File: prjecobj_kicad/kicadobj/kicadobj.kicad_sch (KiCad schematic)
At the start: 39 parts, among them U1 ESP32-S3-DevKitC, U2 PCM1808PWR, U3 MAX9812, U5 PJ-342B

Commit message: feat(prjecobj_kicad)[sang]: update old schematics into new prototype using LTSpice design
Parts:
- removed C1, C2: 0.1uF, Capacitor_SMD:C_0805_2012Metric, symbol Device:C
- removed C10, C14: 10uF, Capacitor_SMD:C_0805_2012Metric, symbol Device:C
- removed C15, C3: 1uF, Capacitor_SMD:C_0805_2012Metric, symbol Device:C
- removed MK1: Microphone, Sensor_Audio:POM-2244P-C3310-2-R, symbol Device:Microphone
- removed MK2: MP45DT02, Sensor_Audio:ST_HLGA-6_3.76x4.72mm_P1.65mm, symbol Sensor_Audio:MP45DT02
- removed unit 2 of Op-amp2
- removed unit 1 of Op-amp2
- removed R1, R14: 2.2kOhm, Resistor_SMD:R_0805_2012Metric, symbol Device:R_US
- removed R10, R11, R4: 10kOhm, Resistor_SMD:R_0805_2012Metric, symbol Device:R_US
- removed R12: 1MOhm, Resistor_SMD:R_0805_2012Metric, symbol Device:R_US
- removed R13, R7: 100kOhm, Resistor_SMD:R_0805_2012Metric, symbol Device:R_US
- removed R15, R5, R6: 1kOhm, Resistor_SMD:R_0805_2012Metric, symbol Device:R_US
- removed U3: MAX9812, max9812:21-0077G, symbol MAX9812:MAX9812
- added C23, C31: 1uF, Capacitor_SMD:C_0805_2012Metric, symbol Device:C
- added C25, C26, C30: 10uF, Capacitor_SMD:C_0805_2012Metric, symbol Device:C
- added C27, C28: 0.1uF, Capacitor_SMD:C_0805_2012Metric, symbol Device:C
- added C29: 1nF, Capacitor_SMD:C_0805_2012Metric, symbol Device:C
- added MK2: Microphone, Sensor_Audio:POM-2244P-C3310-2-R, symbol Device:Microphone
- added Op-amp3: TL072, TL072IDT:SOIC127P600X175-8N, symbol Amplifier_Operational:TL072
- added R26, R27, R29: 100kOhm, Resistor_SMD:R_0805_2012Metric, symbol Device:R_US
- added R28: 2.2kOhm, Resistor_SMD:R_0805_2012Metric, symbol Device:R_US
- added R30: 30kOhm, Resistor_SMD:R_0805_2012Metric, symbol Device:R_US
- added R31: 1kOhm, Resistor_SMD:R_0805_2012Metric, symbol Device:R_US
- added R32: 10kOhm, Resistor_SMD:R_0805_2012Metric, symbol Device:R_US
- added R33, R34: 60kOhm, Resistor_SMD:R_0805_2012Metric, symbol Device:R_US
- added U6: MAX9812, max9812:21-0077G, symbol MAX9812:MAX9812
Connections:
- net 12V: now also R27.1
- net 3.3V: now also C27.1, U6.1 (*SHDN), U6.4 (VCC)
- net GND: now also U5.2, C25.2, C27.2, C29.1, C30.1, C31.2, MK2.1 (-), R28.2, R29.1, U6.2 (GND); no longer U5.3
- net at U2.13 (VINL): now also C13.2, R2.2, R3.1, R33.1, R34.2
- net at U2.14 (VINR): now also C31.1, R34.1
- net at U1.12 (GPIO8/ADC1_CH7): no longer U5.2
- net at U5.4: now also U6.3 (OUT)
- new net: C30.2, R32.1
- new net: C26.1, R33.2
- new net: C26.2, Op-amp3.6 (-), Op-amp3.7
- new net: C25.1, R26.1, R27.2, R29.2
- new net: C23.2, Op-amp3.3 (+), R26.2
- new net: R28.1, U6.5 (BIAS)
- new net: C23.1, U5.3
- new net: C29.2, Op-amp3.5 (+), R31.1
- new net: C28.2, MK2.2 (+)
- new net: C28.1, U6.6 (IN)
- new net: Op-amp3.2 (-), R30.2, R32.2
- new net: Op-amp3.1, R30.1, R31.2
- no-connect marks 38 -> 41
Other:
- moved on the sheet: Op-amp2C, U5

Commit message: feat(kicad): update schematics and ad new PCB design with remove PCM1808 item and replace with pin connector
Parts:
- removed C27, C28, C5, C7, C9: 0.1uF, Capacitor_SMD:C_0805_2012Metric, symbol Device:C
- removed C4, C6, C8: 10uF, Capacitor_SMD:C_0805_2012Metric, symbol Device:C
- removed MK2: Microphone, Sensor_Audio:POM-2244P-C3310-2-R, symbol Device:Microphone
- removed Op-amp2: TL072, TL072IDT:SOIC127P600X175-8N, symbol Amplifier_Operational:TL072
- removed R28: 2.2kOhm, Resistor_SMD:R_0805_2012Metric, symbol Device:R_US
- removed U1: ESP32-S3-DevKitC, PCM_Espressif:ESP32-S3-DevKitC, symbol PCM_Espressif:ESP32-S3-DevKitC
- removed U2: PCM1808PWR, pcm1808-pwr:SOP65P640X120-14N, symbol PCM1808PWR:PCM1808PWR
- removed U6: MAX9812, max9812:21-0077G, symbol MAX9812:MAX9812
- added J1: MAX9812_Con_Pin_0103_V, Connector_PinHeader_2.54mm:PinHeader_1x03_P2.54mm_Vertical, symbol Connector_Generic:Conn_01x03
- added J2, J3: Conn_01x05, Connector_PinHeader_2.54mm:PinHeader_1x05_P2.54mm_Vertical, symbol Connector_Generic:Conn_01x05
- added J4: PCM1808_Con_Pin_0103_V, Connector_PinHeader_2.54mm:PinHeader_1x03_P2.54mm_Vertical, symbol Connector_Generic:Conn_01x03
- added unit 3 of Op-amp3
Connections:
- net 12V: now also Op-amp3.8 (V+)
- net 3.3V: now also J1.1 (Pin_1), J2.4 (Pin_4), J3.1 (Pin_1)
- net 5V: now also J2.5 (Pin_5)
- net GND: now also J2.3 (Pin_3), J3.2 (Pin_2), Op-amp3.4 (V-)
- net at C13.2, R2.2, R3.1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: now also J4.1 (Pin_1)
- net at C31.1, R34.1: now also J4.3 (Pin_3)
- net at INVBUF1.4, R8.2, R9.2: now also J3.3 (Pin_3)
- net at U5.4: now also J1.3 (Pin_3)
- no-connect marks 41 -> 16
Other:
- note added: "+3.3"
- note added: "+5"
- note added: "BCK"
- note added: "GND"
- note added: "LIN"
- note added: "LRC"
- note added: "MD0"
- note added: "MD1"
- note added: "OUT"
- note added: "PMT"
- note added: "RIN"
- note added: "SCK"

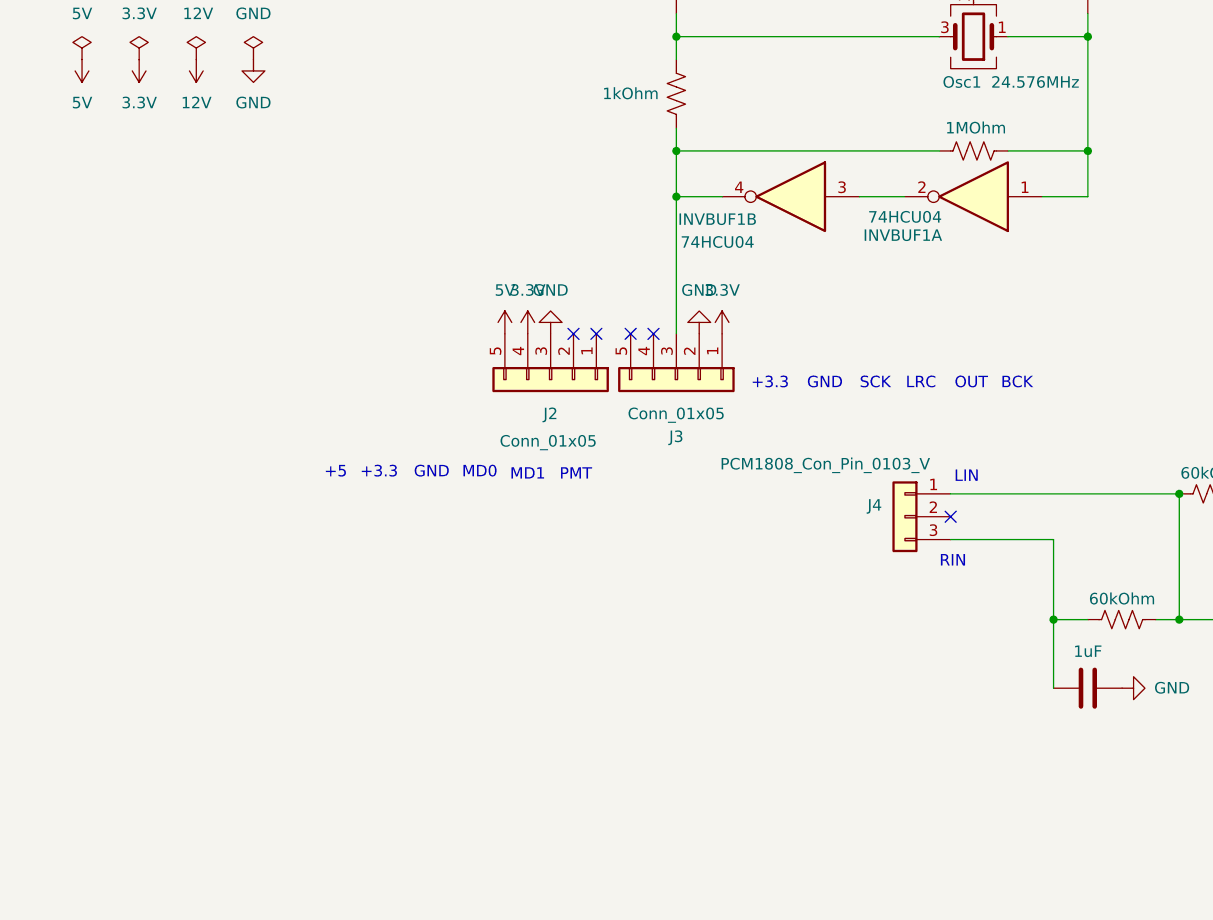
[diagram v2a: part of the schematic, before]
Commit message: feat(kicad): update connector from 1x5 to 1x6 with adding net
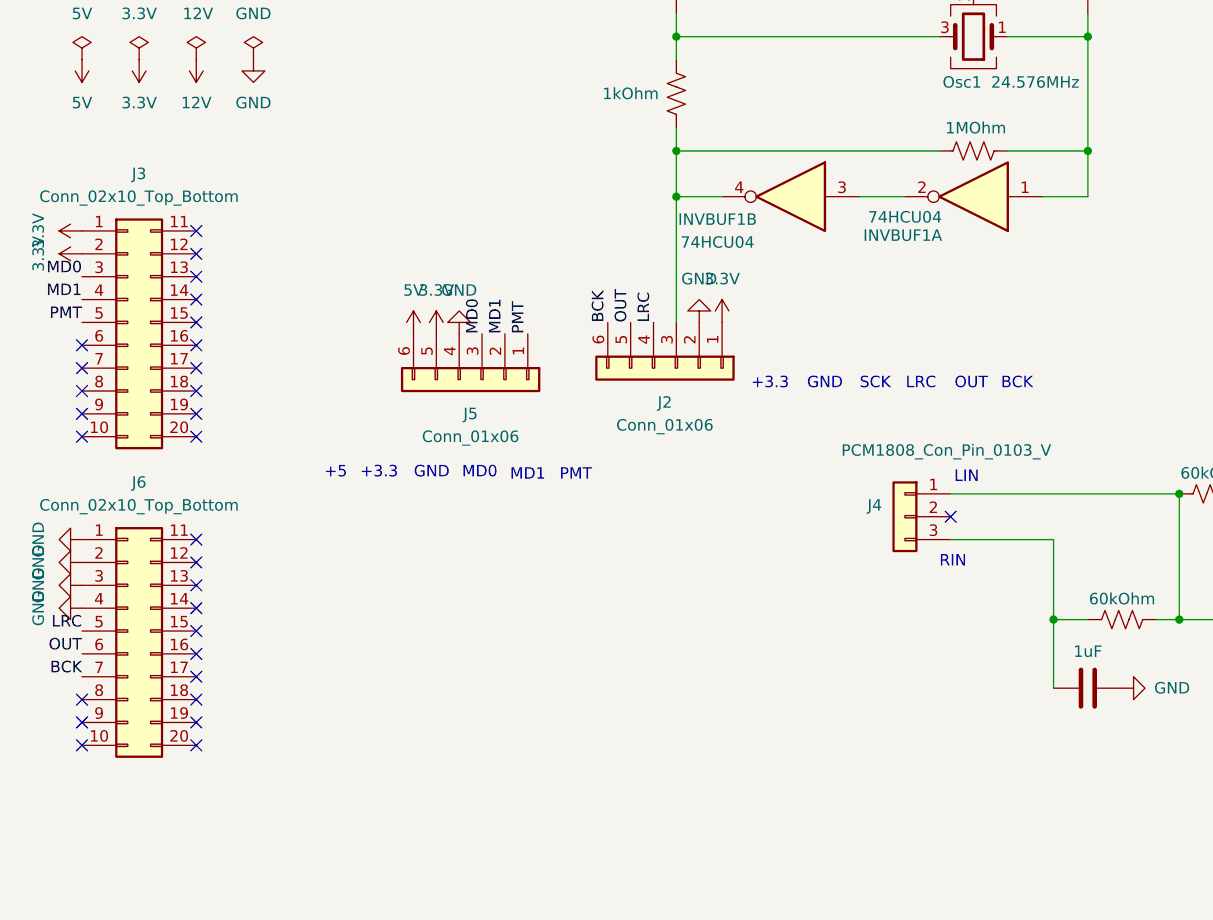
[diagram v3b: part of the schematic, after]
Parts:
- removed J2, J3: Conn_01x05, Connector_PinHeader_2.54mm:PinHeader_1x05_P2.54mm_Vertical, symbol Connector_Generic:Conn_01x05
- added J2, J5: Conn_01x06, Connector_PinHeader_2.54mm:PinHeader_1x06_P2.54mm_Vertical, symbol Connector_Generic:Conn_01x06
- added J3, J6: Conn_02x10_Top_Bottom, Connector_PinSocket_2.54mm:PinSocket_2x10_P2.54mm_Vertical, symbol Connector_Generic:Conn_02x10_Top_Bottom
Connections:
- net 3.3V: now also J2.1 (Pin_1), J3.1 (Pin_1), J3.2 (Pin_2), J5.5 (Pin_5)
- net 5V: now also J5.6 (Pin_6)
- net GND: now also J2.2 (Pin_2), J5.4 (Pin_4), J6.1 (Pin_1), J6.2 (Pin_2), J6.3 (Pin_3), J6.4 (Pin_4)
- net at INVBUF1.4, R8.2, R9.2: now also J2.3 (Pin_3)
- new net BCK: J2.6 (Pin_6), J6.7 (Pin_7)
- new net LRC: J2.4 (Pin_4), J6.5 (Pin_5)
- new net MD0: J3.3 (Pin_3), J5.3 (Pin_3)
- new net MD1: J3.4 (Pin_4), J5.2 (Pin_2)
- new net OUT: J2.5 (Pin_5), J6.6 (Pin_6)
- new net PMT: J3.5 (Pin_5), J5.1 (Pin_1)
- no-connect marks 16 -> 40
